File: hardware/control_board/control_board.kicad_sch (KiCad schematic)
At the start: 0 parts

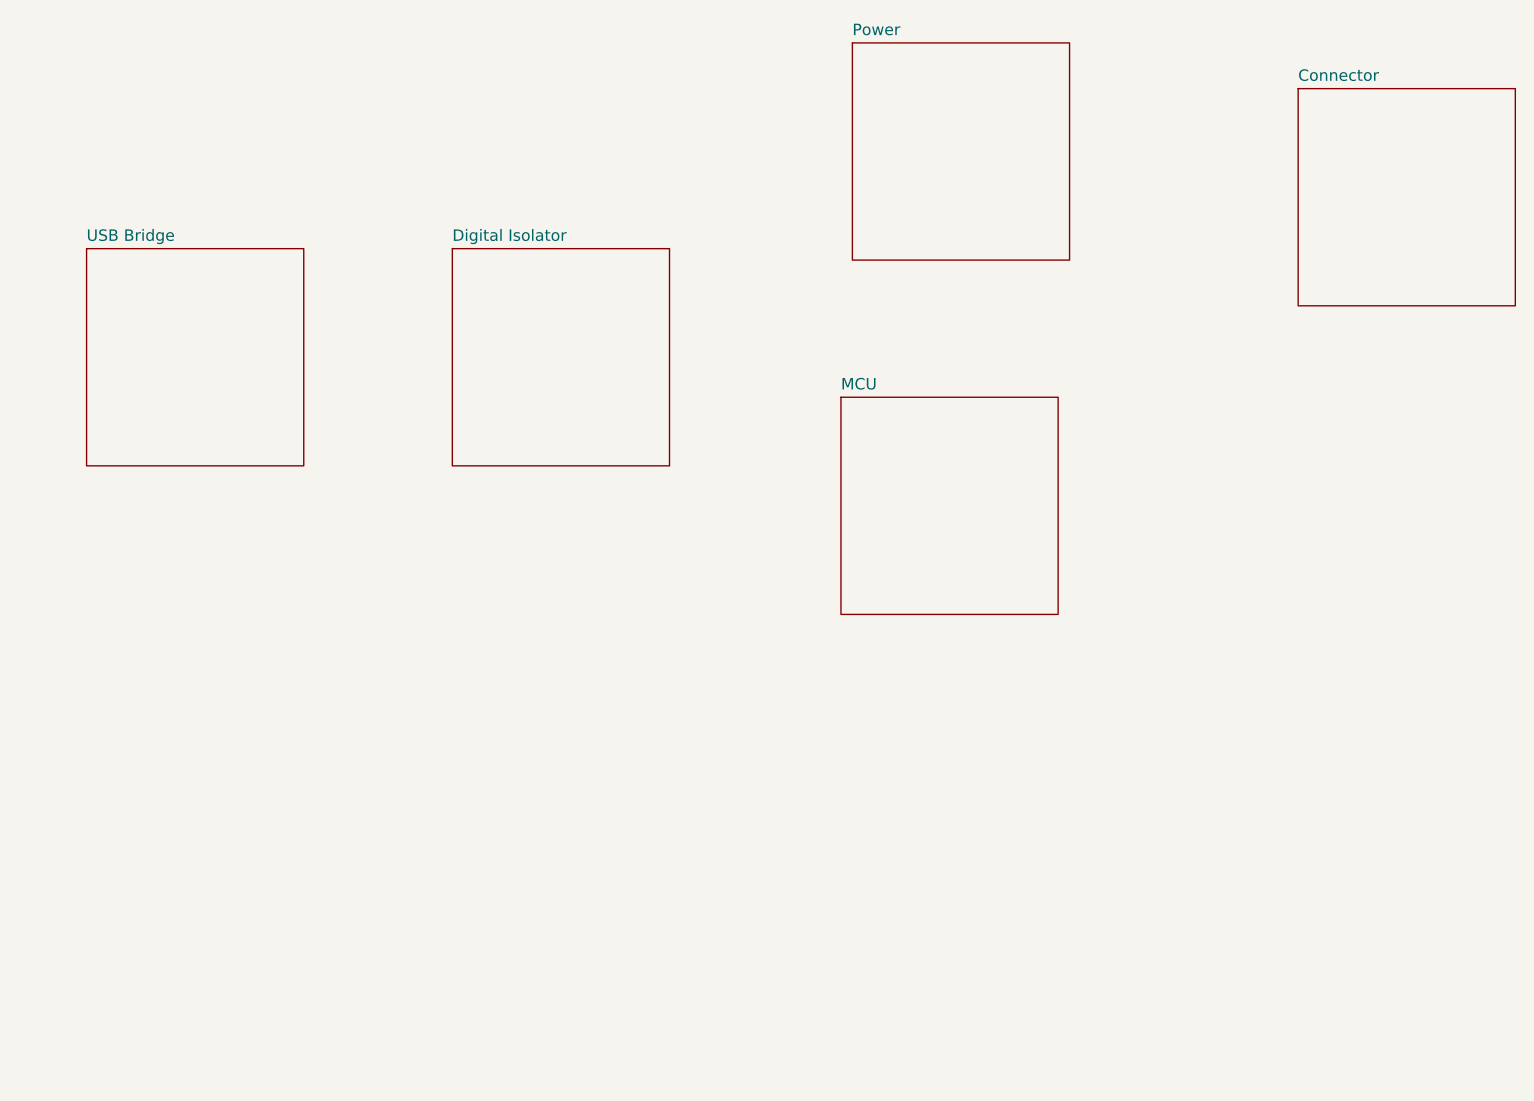
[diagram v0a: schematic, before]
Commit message: added symbols and footprints
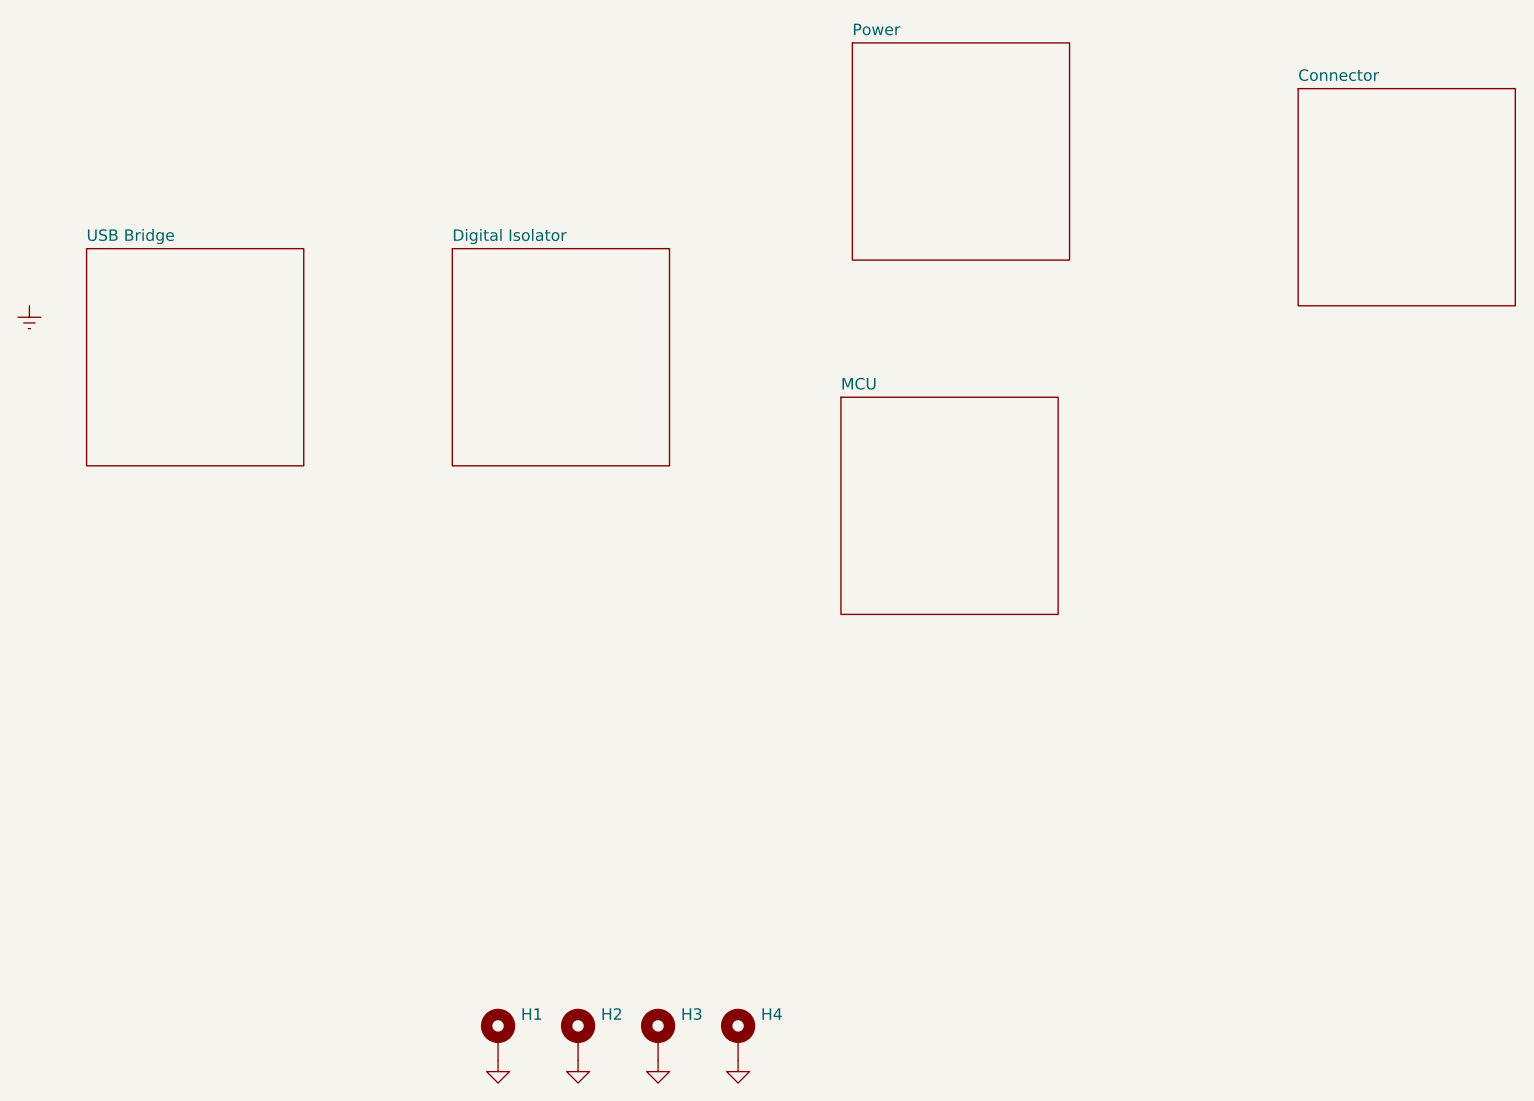
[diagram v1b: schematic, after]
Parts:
- added H1, H2, H3, H4: MountingHole_Pad, MountingHole:MountingHole_3.2mm_M3_Pad_Via, symbol Mechanical:MountingHole_Pad
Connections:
- new net GND: H1.1, H2.1, H3.1, H4.1
